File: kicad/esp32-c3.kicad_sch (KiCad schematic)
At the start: 19 parts, among them U1 SN65HVD230, U5 ESP32-C3-MINI-1

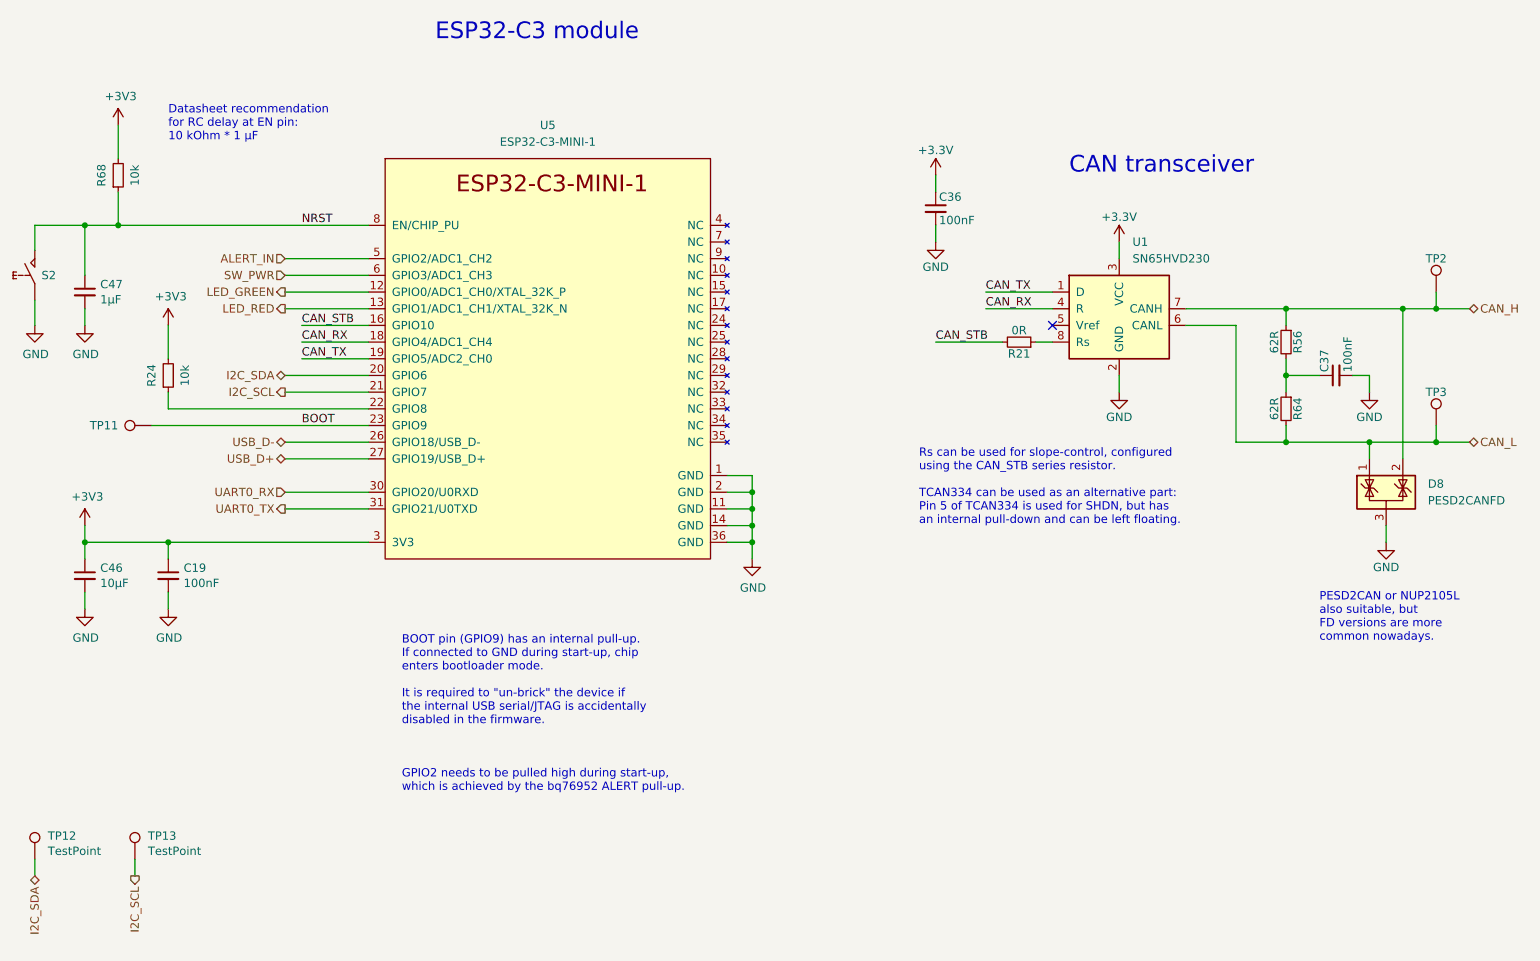
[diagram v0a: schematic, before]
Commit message: v0.4.0: Multiple improvements for new board revision
- Use LMR38010 for internal power supply (max. 80V instead of 60V)
- Change USB connector from Micro-A to C and remove 5V power supply
  which was not working anyway. The board cannot be powered by USB
  only.
- Add TS2 (connected to DFETOFF) to measure shunt temperature
- Add RS-485 transceiver (sharing the connector with CAN)
- Switch I2C pins of ESP32-C3 to GPIO8/9. This allows to re-use the
  I2C pull-ups for strapping configuration and frees two pins for the
  RS-485 transceiver RE and DE pins. Also we may get rid of the I2C
  glitches during start-up.
- Reduce DSG gate resistor R57 to 47R to increase switch-off speed.
- Use more easily available and cheaper Würth 7466005R terminals with
  countersunk hole/thread.
- Adjust some resistors to reduce number of different parts
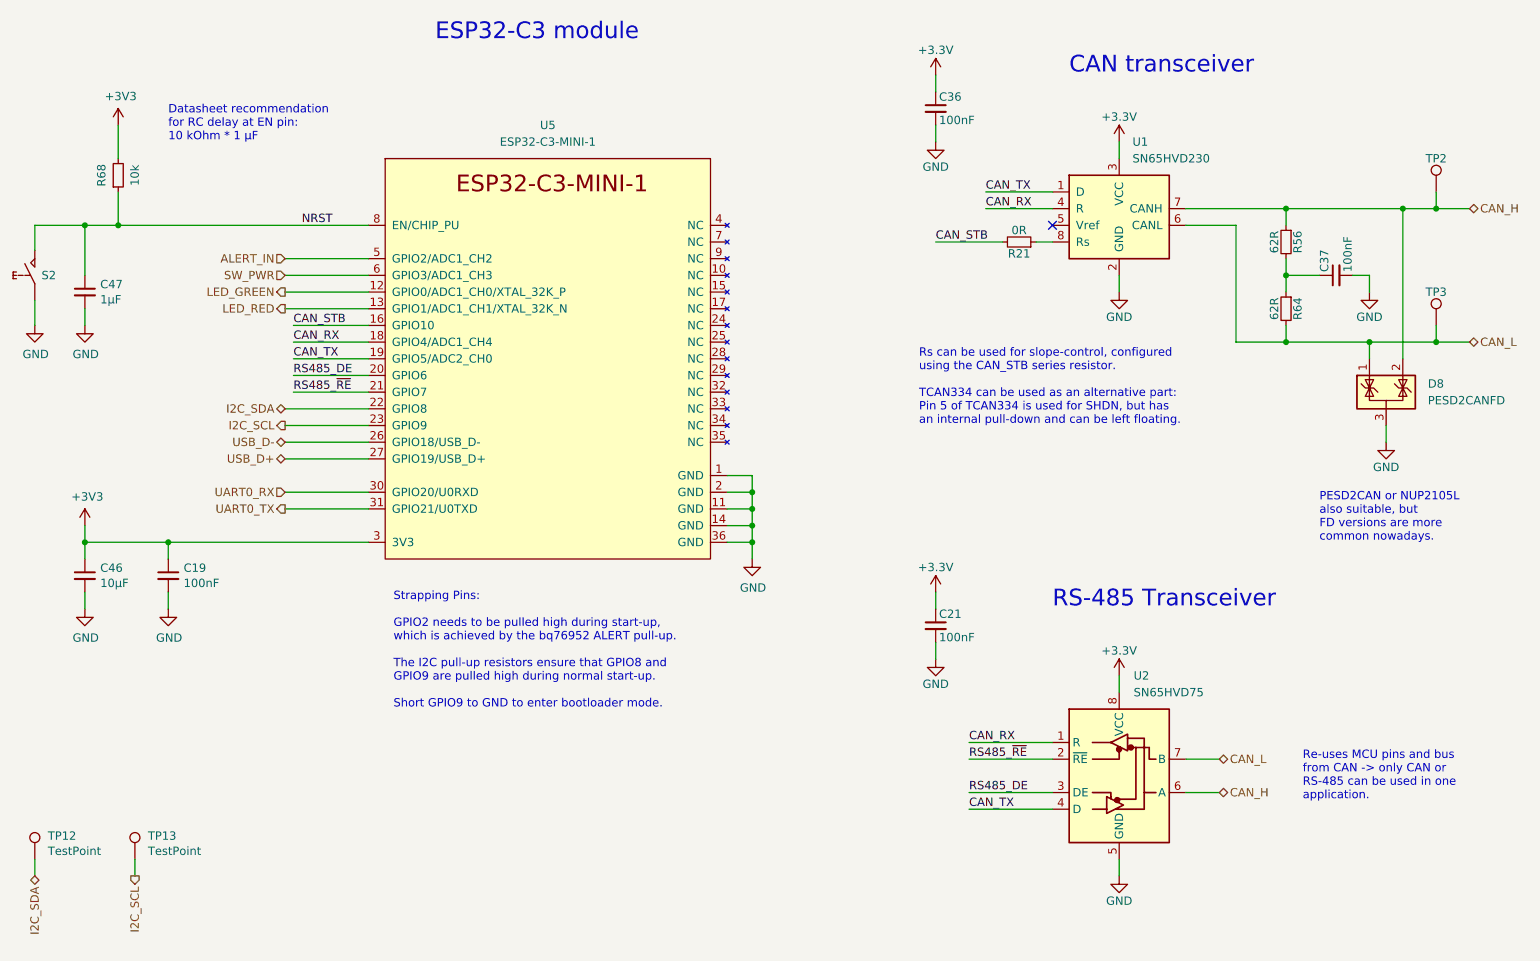
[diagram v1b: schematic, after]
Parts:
- removed R24: 10k, LibreSolar:R_0603_1608, symbol LibreSolar:R
- removed TP11: TestPoint, TestPoint:TestPoint_Pad_D1.5mm, symbol Connector:TestPoint
- added C21: 100nF, LibreSolar:C_0603_1608, symbol LibreSolar:C
- added U2: SN65HVD75, Package_SO:SOIC-8_3.9x4.9mm_P1.27mm, symbol Interface_UART:SN65HVD11HD
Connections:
- net BOOT is gone; now on net I2C_SCL: U5.23 (GPIO9)
- net +3V3: now also C21.1, U2.8 (VCC)
- net CAN_H: now also U2.6 (A)
- net CAN_L: now also U2.7 (B)
- net CAN_RX: now also U2.1 (R)
- net CAN_TX: now also U2.4 (D)
- net GND: now also C21.2, U2.5 (GND)
- net I2C_SCL: no longer U5.21 (GPIO7)
- net I2C_SDA: now also U5.22 (GPIO8); no longer U5.20 (GPIO6)
- new net RS485_DE: U2.3 (DE), U5.20 (GPIO6)
- new net RS485_~{RE}: U2.2 (~{RE}), U5.21 (GPIO7)
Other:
- note added: "RS-485 Transceiver"
- note added: "Re-uses MCU pins and bus from CAN -> only CAN or RS-485 can be used in one application."
- note added: "Strapping Pins: GPIO2 needs to be pulled high during start-up, which is achieved by the bq76952 ALERT pull-up. The I2C pull-up resistors ensure that GPIO8 and GPIO9 are pulled high during normal start-up. Short GPIO9 to GND to enter bootloader mode."
- note removed: "BOOT pin (GPIO9) has an internal pull-up. If connected to GND during start-up, chip enters bootloader mode. It is required to "un-brick" the device if the internal USB serial/JTAG is accidentally disabled in the firmware."
- note removed: "GPIO2 needs to be pulled high during start-up, which is achieved by the bq76952 ALERT pull-up."
- moved on the sheet: C36, C37, D8, R21, R56, R64, TP2, TP3, U1
